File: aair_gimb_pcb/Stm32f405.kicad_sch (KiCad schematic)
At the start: 17 parts, among them J3 USB_B_Mini, J4 SWD, U2 STM32F405RGTx, U4 USBLC6-2SC6, X2 8MHz

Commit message: macros
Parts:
- C11, C13, C14, C15, C16: footprint (none) -> CRF1:SMD-0603_r
- C12: footprint (none) -> CRF1:SMD-0603_c
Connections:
- net GND: now also U2.12 (VSSA), U2.18 (VSS), U2.63 (VSS)
- net L3: now reaches U2.34 (PB13)
- net L2: now reaches U2.35 (PB14)
- net L1: now reaches U2.36 (PB15)
- net H1: now reaches U2.41 (PA8)
- net H2: now reaches U2.42 (PA9)
- net H3: now reaches U2.43 (PA10)
- net SWO: no longer names the net of U2.55 (PB3)
- net SWO: no longer J4.6 (Pin_6)
- no-connect marks 4 -> 5
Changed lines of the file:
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@@
 	)
 	(no_connect
+		(at 243.84 107.95)
+	)
+	(no_connect
 		(at 193.04 138.43)
 	)
@@
 		)
 	)
-	(global_label "SWO"
-		(shape input)
-		(at 165.1 113.03 0)
-		(effects
-			(font
-				(size 1.27 1.27)
-			)
-			(justify left)
-		)
-		(property "Intersheetrefs" "${INTERSHEET_REFS}"
-			(at 165.1 113.03 0)
-			(effects
-				(font
-					(size 1.27 1.27)
-				)
-				(hide yes)
-			)
-		)
-	)
 	(global_label "SWDIO"
 		(shape input)
@@
 		)
 	)
-	(global_label "SWO"
-		(shape input)
-		(at 243.84 107.95 0)
-		(effects
-			(font
-				(size 1.27 1.27)
-			)
-			(justify left)
-		)
-		(property "Intersheetrefs" "${INTERSHEET_REFS}"
-			(at 243.84 107.95 0)
-			(effects
-				(font
-					(size 1.27 1.27)
-				)
-				(hide yes)
-			)
-		)
-	)
 	(global_label "LED_STATUS"
 		(shape input)
@@
 		)
 	)
+	(hierarchical_label "L2"
+		(shape output)
+		(at 165.1 140.97 0)
+		(effects
+			(font
+				(size 1.27 1.27)
+			)
+			(justify left)
+		)
+	)
+	(hierarchical_label "H3"
+		(shape output)
+		(at 165.1 87.63 0)
+		(effects
+			(font
+				(size 1.27 1.27)
+			)
+			(justify left)
+		)
+	)
+	(hierarchical_label "H2"
+		(shape output)
+		(at 165.1 85.09 0)
+		(effects
+			(font
+				(size 1.27 1.27)
+			)
+			(justify left)
+		)
+	)
+	(hierarchical_label "L1"
+		(shape output)
+		(at 165.1 143.51 0)
+		(effects
+			(font
+				(size 1.27 1.27)
+			)
+			(justify left)
+		)
+	)
+	(hierarchical_label "H1"
+		(shape output)
+		(at 165.1 82.55 0)
+		(effects
+			(font
+				(size 1.27 1.27)
+			)
+			(justify left)
+		)
+	)
+	(hierarchical_label "L3"
+		(shape output)
+		(at 165.1 138.43 0)
+		(effects
+			(font
+				(size 1.27 1.27)
+			)
+			(justify left)
+		)
+	)
 	(symbol
 		(lib_id "Device:C_Small")
@@
 			)
 		)
-		(property "Footprint" ""
+		(property "Footprint" "CRF1:SMD-0603_r"
 			(at 111.76 128.27 0)
 			(effects
@@
 			)
 		)
-		(property "Footprint" ""
+		(property "Footprint" "CRF1:SMD-0603_r"
 			(at 153.67 43.18 0)
 			(effects
@@
 	(symbol
 		(lib_id "power:GND")
+		(at 140.97 157.48 0)
+		(unit 1)
+		(exclude_from_sim no)
+		(in_bom yes)
+		(on_board yes)
+		(dnp no)
+		(fields_autoplaced yes)
+		(property "Reference" "#PWR04"
+			(at 140.97 163.83 0)
+			(effects
+				(font
+					(size 1.27 1.27)
+				)
+				(hide yes)
+			)
+		)
+		(property "Value" "GND"
+			(at 140.97 162.56 0)
+			(effects
+				(font
+					(size 1.27 1.27)
+				)
+			)
+		)
+		(property "Footprint" ""
+			(at 140.97 157.48 0)
+			(effects
+				(font
+					(size 1.27 1.27)
+				)
+				(hide yes)
+			)
+		)
+		(property "Datasheet" ""
+			(at 140.97 157.48 0)
+			(effects
+				(font
+					(size 1.27 1.27)
+				)
+				(hide yes)
+			)
+		)
+		(property "Description" "Power symbol creates a global label with name \"GND\" , ground"
+			(at 140.97 157.48 0)
+			(effects
+				(font
+					(size 1.27 1.27)
+				)
+				(hide yes)
+			)
+		)
+		(pin "1"
+		)
+		(instances
+			(project ""
+				(path "/d04c5395-2e3c-40b8-8677-11fb81ced555/7fbb9adf-0048-4876-8c48-9f0d8db4e360"
+					(reference "#PWR04")
+					(unit 1)
+				)
+			)
+		)
+	)
+	(symbol
+		(lib_id "power:GND")
 		(at 185.42 143.51 0)
 		(unit 1)
@@
 			)
 		)
-		(property "Footprint" ""
+		(property "Footprint" "CRF1:SMD-0603_r"
 			(at 158.75 43.18 0)
 			(effects
@@
 			)
 		)
-		(property "Footprint" ""
+		(property "Footprint" "CRF1:SMD-0603_c"
 			(at 111.76 134.62 0)
 			(effects
@@
 			)
 		)
-		(property "Footprint" ""
+		(property "Footprint" "CRF1:SMD-0603_r"
 			(at 168.91 43.18 0)
 			(effects
@@
 			)
 		)
-		(property "Footprint" ""
+		(property "Footprint" "CRF1:SMD-0603_r"
 			(at 163.83 43.18 0)
 			(effects

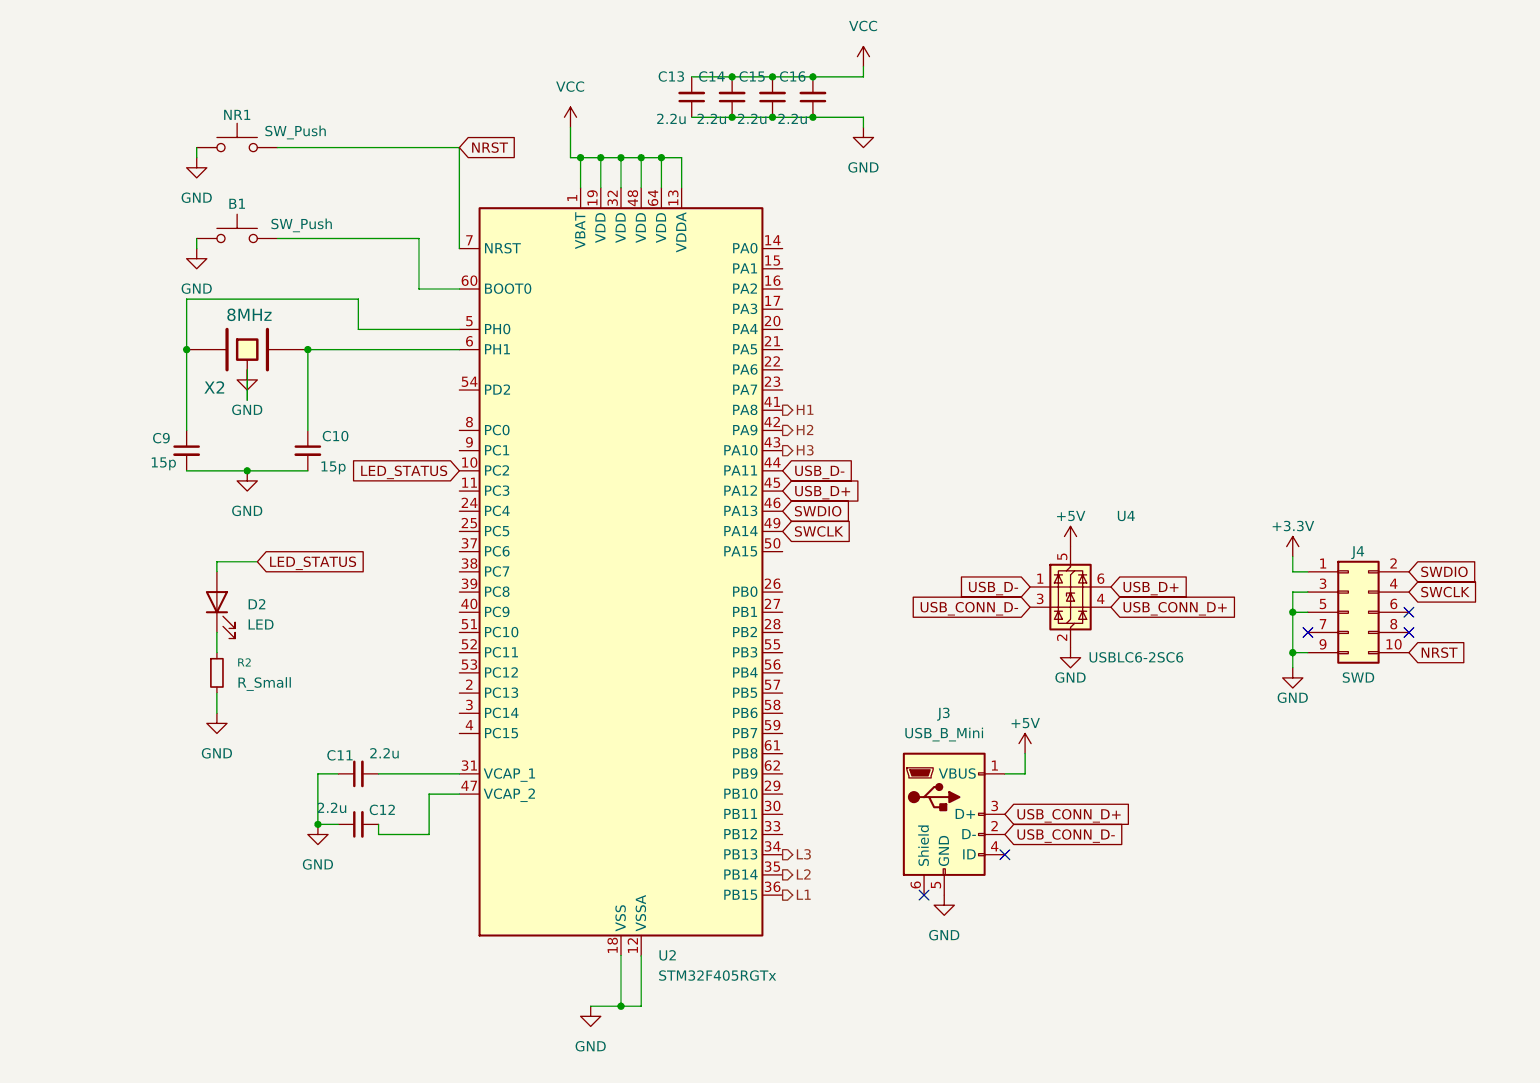
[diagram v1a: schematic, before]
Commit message: добавить пины стм, диод, питание 3.3, разъемы
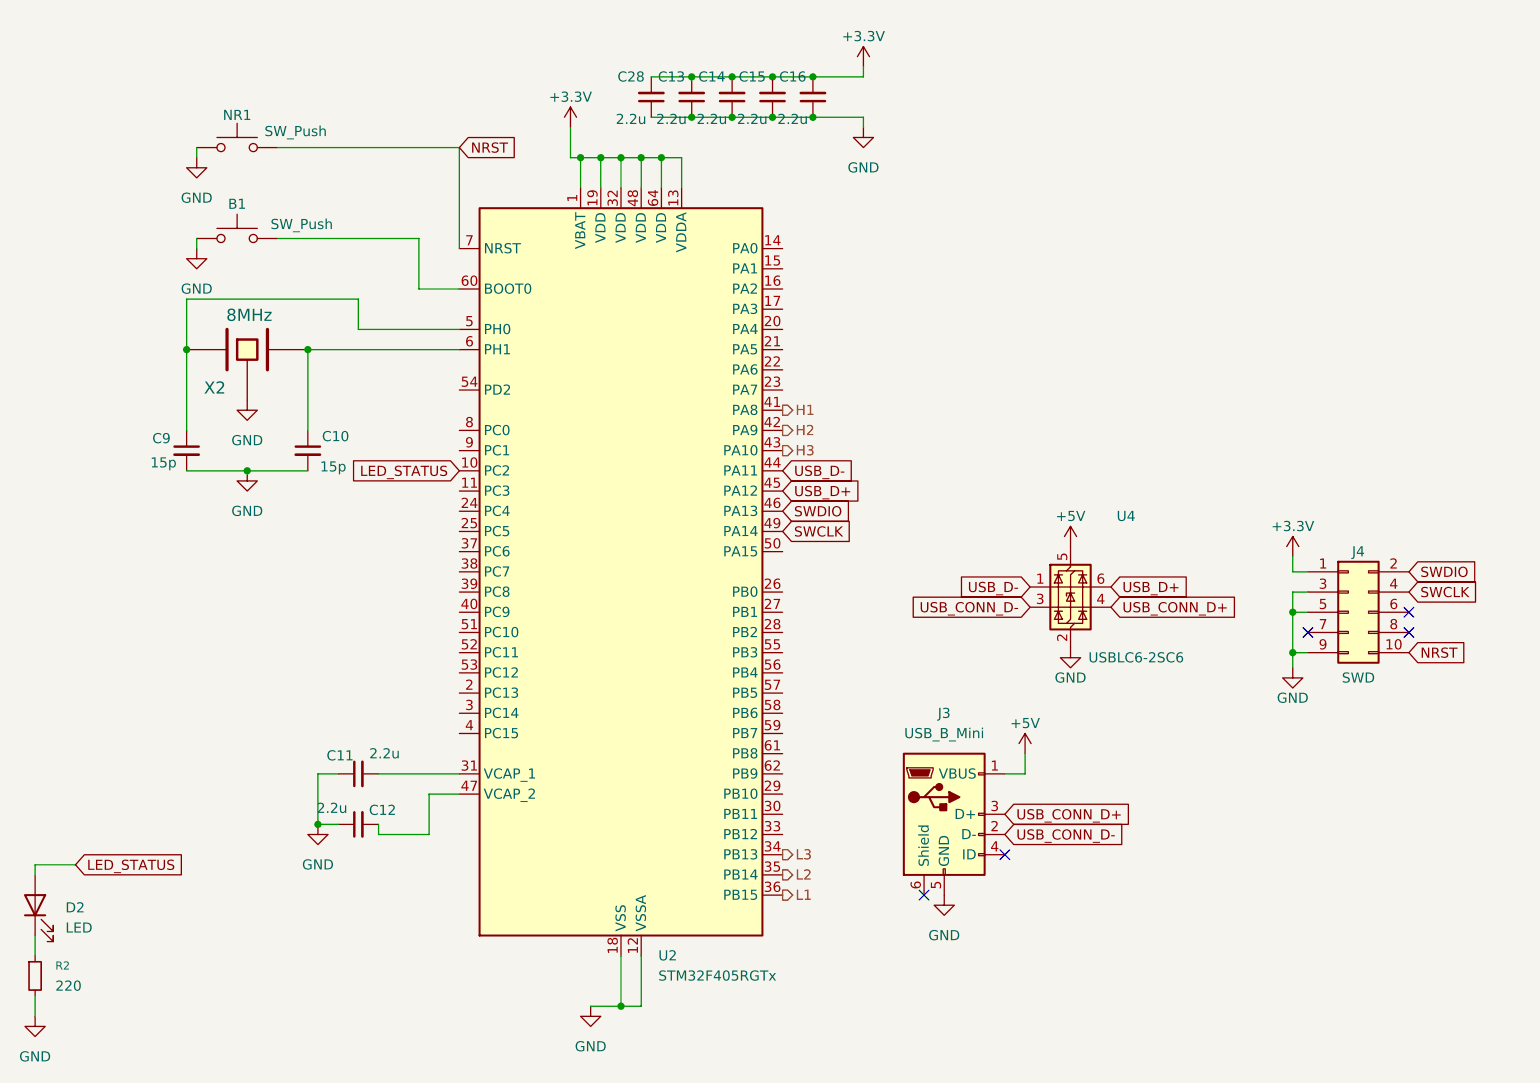
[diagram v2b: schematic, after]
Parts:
- added C28: 2.2u, CRF1:SMD-0603_c, symbol Device:C_Small
- C11, C13, C14, C15, C16: footprint CRF1:SMD-0603_r -> CRF1:SMD-0603_c
- R2: value R_Small -> 220
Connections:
- net VCC is gone; now on net +3.3V: C13.2, C14.2, C15.2, C16.2, U2.1 (VBAT), U2.13 (VDDA), U2.19 (VDD), U2.32 (VDD), U2.48 (VDD), U2.64 (VDD)
- net +3.3V: now also C28.2
- net GND: now also C28.1
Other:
- moved on the sheet: D2, R2

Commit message: сделать коннектор для переыерии
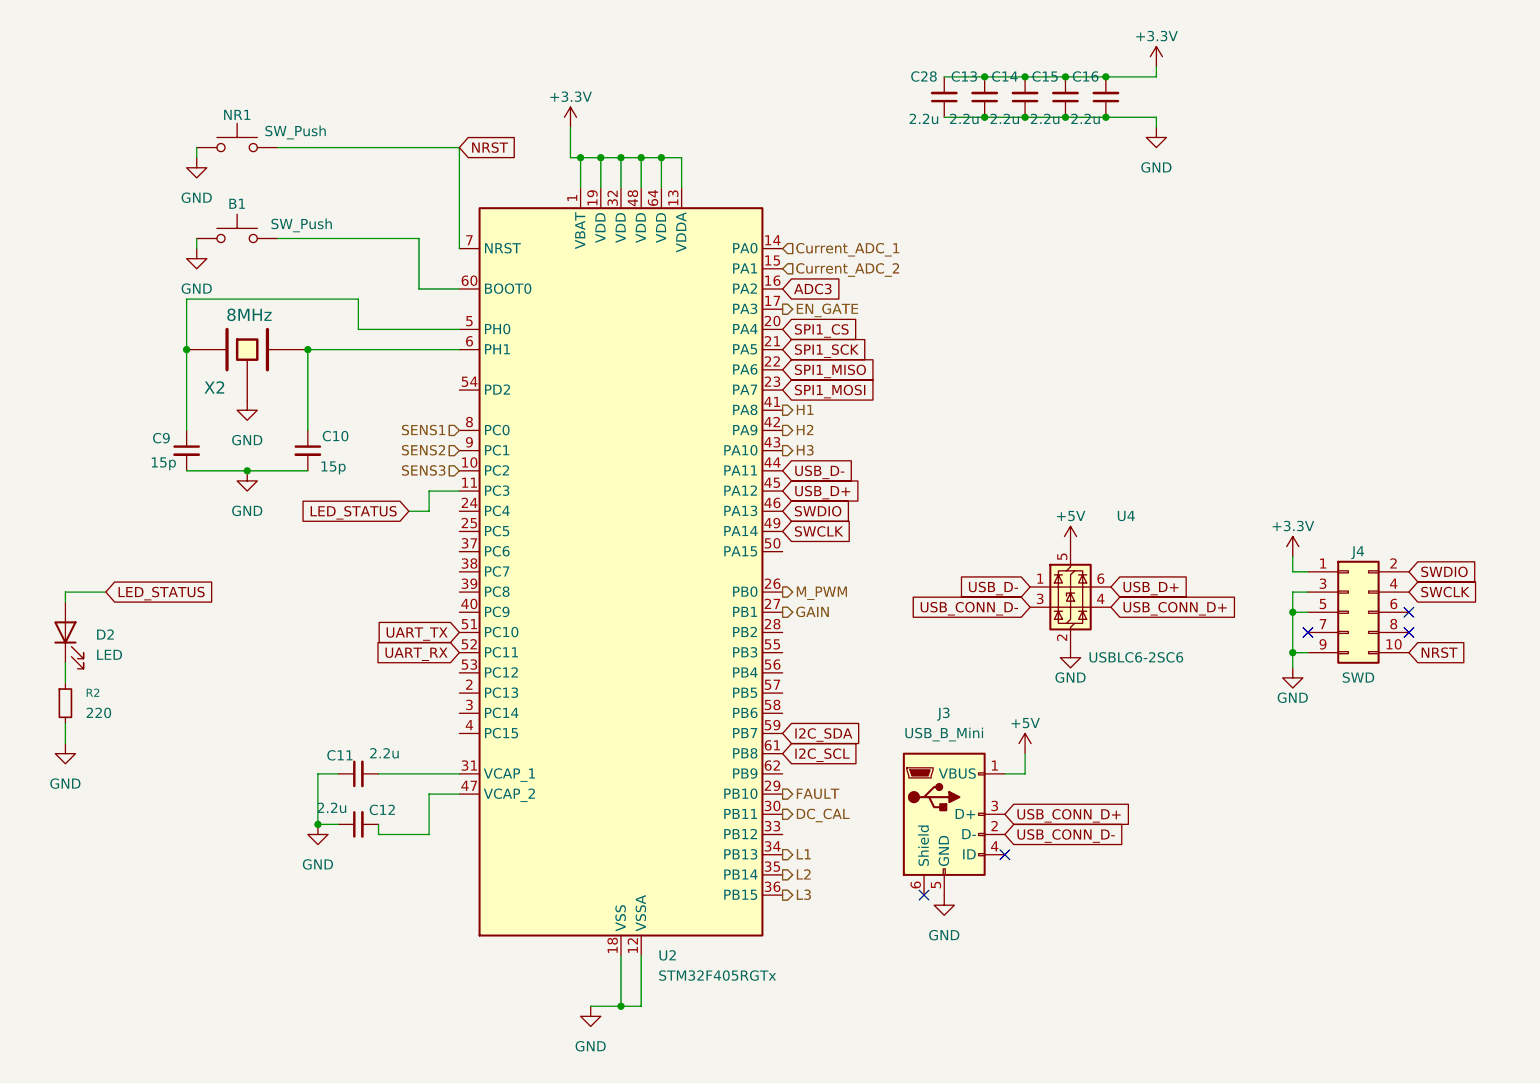
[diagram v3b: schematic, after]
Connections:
- net L1: now also U2.34 (PB13); no longer U2.36 (PB15)
- net L3: now also U2.36 (PB15); no longer U2.34 (PB13)
- net LED_STATUS: now also U2.11 (PC3); no longer U2.10 (PC2)
- net Current_ADC_1: now reaches U2.14 (PA0)
- net Current_ADC_2: now reaches U2.15 (PA1)
- net ADC3: now reaches U2.16 (PA2)
- net EN_GATE: now reaches U2.17 (PA3)
- net SPI1_CS: now reaches U2.20 (PA4)
- net SPI1_SCK: now reaches U2.21 (PA5)
- net SPI1_MISO: now reaches U2.22 (PA6)
- net SPI1_MOSI: now reaches U2.23 (PA7)
- net M_PWM: now reaches U2.26 (PB0)
- net GAIN: now reaches U2.27 (PB1)
- net FAULT: now reaches U2.29 (PB10)
- net DC_CAL: now reaches U2.30 (PB11)
- net UART_TX: now reaches U2.51 (PC10)
- net UART_RX: now reaches U2.52 (PC11)
- net I2C_SDA: now reaches U2.59 (PB7)
- net I2C_SCL: now reaches U2.61 (PB8)
- net SENS1: now reaches U2.8 (PC0)
- net SENS2: now reaches U2.9 (PC1)
- new net SENS3: U2.10 (PC2)
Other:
- moved on the sheet: C13, C14, C15, C16, C28, D2, R2

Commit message: pcb
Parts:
- added J1: I2C, Connector_JST:JST_GH_BM04B-GHS-TBT_1x04-1MP_P1.25mm_Vertical, symbol Connector:Conn_01x04_Pin
- added J2: UART, Connector_JST:JST_GH_BM04B-GHS-TBT_1x04-1MP_P1.25mm_Vertical, symbol Connector:Conn_01x04_Pin
- added J6: SPI1, Connector_JST:JST_GH_BM06B-GHS-TBT_1x06-1MP_P1.25mm_Vertical, symbol Connector:Conn_01x06_Pin
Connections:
- net +3.3V: now also J1.4 (Pin_4), J2.4 (Pin_4), J6.6 (Pin_6)
- net ADC3: now also U2.14 (PA0); no longer U2.16 (PA2)
- net Current_ADC_1: now also U2.16 (PA2); no longer U2.14 (PA0)
- net GND: now also J1.3 (Pin_3), J2.3 (Pin_3), J6.5 (Pin_5)
- net I2C_SCL: now also J1.1 (Pin_1)
- net I2C_SDA: now also J1.2 (Pin_2)
- net SPI1_CS: now also J6.4 (Pin_4)
- net SPI1_MISO: now also J6.2 (Pin_2)
- net SPI1_MOSI: now also J6.1 (Pin_1)
- net SPI1_SCK: now also J6.3 (Pin_3)
- net UART_RX: now also J2.1 (Pin_1)
- net UART_TX: now also J2.2 (Pin_2)
- no-connect marks 5 -> 24

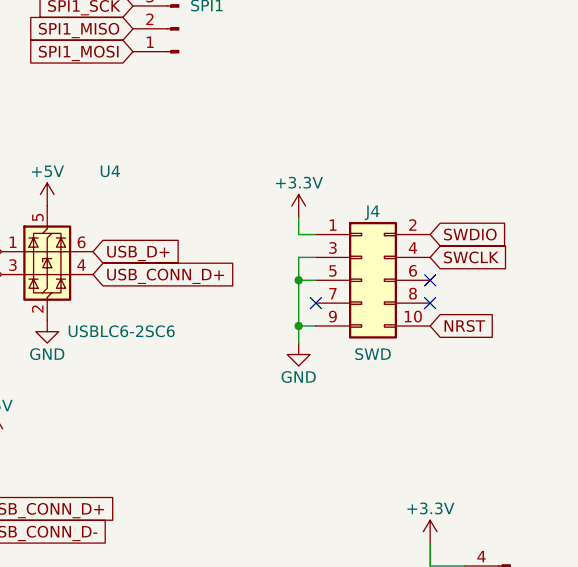
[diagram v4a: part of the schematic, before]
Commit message: add digital logic to pcb
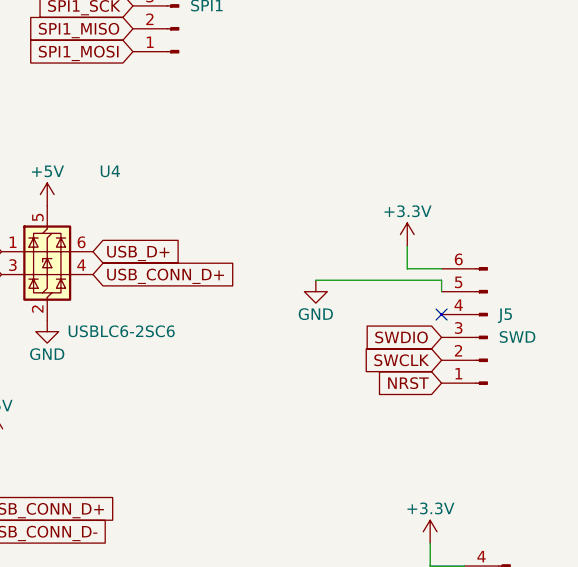
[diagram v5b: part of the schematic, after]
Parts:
- removed J4: SWD, Connector_PinHeader_1.27mm:PinHeader_2x05_P1.27mm_Vertical_SMD, symbol Connector_Generic:Conn_02x05_Odd_Even
- added J5: SWD, Connector_JST:JST_GH_BM06B-GHS-TBT_1x06-1MP_P1.25mm_Vertical, symbol Connector:Conn_01x06_Pin
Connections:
- net +3.3V: now also J5.6 (Pin_6)
- net GND: now also J5.5 (Pin_5)
- net NRST: now also J5.1 (Pin_1)
- net SWCLK: now also J5.2 (Pin_2)
- net SWDIO: now also J5.3 (Pin_3)
- no-connect marks 24 -> 22

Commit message: готово
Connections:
- net GND: now also J3.6 (Shield)
- no-connect marks 22 -> 21
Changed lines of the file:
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@@
-	)
-	(no_connect
-		(at 182.88 143.51)
 	)
 	(no_connect
@@
 		(pts
 			(xy 105.41 74.93) (xy 124.46 74.93)
+		)
+		(stroke
+			(width 0)
+			(type default)
+		)
+	)
+	(wire
+		(pts
+			(xy 180.34 143.51) (xy 182.88 143.51)
 		)
 		(stroke
@@
 					(unit 1)
 				)
+			)
+		)
+	)
+	(symbol
+		(lib_id "power:GND")
+		(at 180.34 143.51 0)
+		(unit 1)
+		(exclude_from_sim no)
+		(in_bom yes)
+		(on_board yes)
+		(dnp no)
+		(fields_autoplaced yes)
+		(property "Reference" "#PWR027"
+			(at 180.34 149.86 0)
+			(effects
+				(font
+					(size 1.27 1.27)
+				)
+				(hide yes)
+			)
+		)
+		(property "Value" "GND"
+			(at 180.34 148.59 0)
+			(effects
+				(font
+					(size 1.27 1.27)
+				)
+			)
+		)
+		(property "Footprint" ""
+			(at 180.34 143.51 0)
+			(effects
+				(font
+					(size 1.27 1.27)
+				)
+				(hide yes)
+			)
+		)
+		(property "Datasheet" ""
+			(at 180.34 143.51 0)
+			(effects
+				(font
+					(size 1.27 1.27)
+				)
+				(hide yes)
+			)
+		)
+		(property "Description" "Power symbol creates a global label with name \"GND\" , ground"
+			(at 180.34 143.51 0)
+			(effects
+				(font
+					(size 1.27 1.27)
+				)
+				(hide yes)
+			)
+		)
+		(pin "1"
+		)
+		(instances
+			(project "aair_gimb_pcb"
+				(path "/d04c5395-2e3c-40b8-8677-11fb81ced555/7fbb9adf-0048-4876-8c48-9f0d8db4e360"
+					(reference "#PWR027")
+					(unit 1)
+				)
